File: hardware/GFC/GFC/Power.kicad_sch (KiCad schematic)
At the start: 8 parts

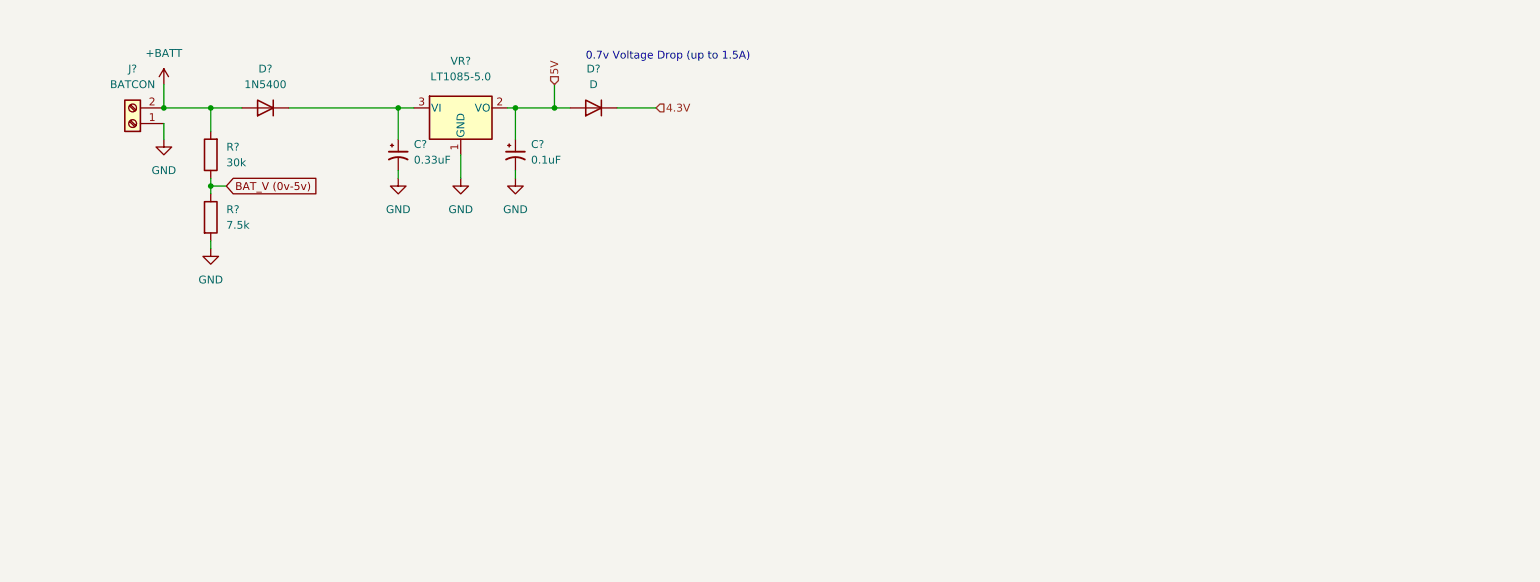
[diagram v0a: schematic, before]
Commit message: Some hardware changes, started to add footprints and part links to digikey. Switching most to SMD
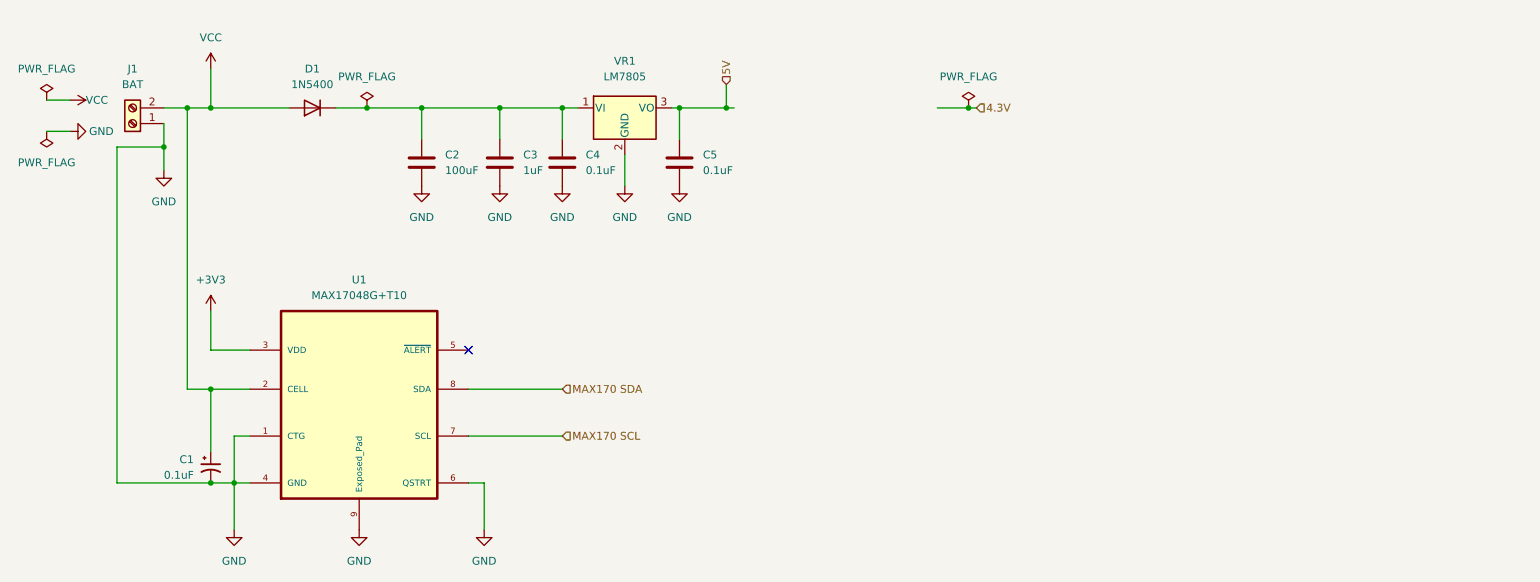
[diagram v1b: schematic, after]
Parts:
- removed C?: 0.1uF, symbol Device:C_Polarized_Small_US
- removed C?: 0.33uF, symbol Device:C_Polarized_Small_US
- removed D?: D, symbol Device:D
- removed R?: 7.5k, symbol Device:R
- removed R?: 30k, symbol Device:R
- added C1: 0.1uF, Capacitor_SMD:C_0603_1608Metric_Pad1.08x0.95mm_HandSolder, symbol Device:C_Polarized_Small_US
- added C2: 100uF, Capacitor_THT:CP_Radial_D6.3mm_P2.50mm, symbol Device:C
- added C3: 1uF, Capacitor_SMD:C_0603_1608Metric_Pad1.08x0.95mm_HandSolder, symbol Device:C
- added C4, C5: 0.1uF, Capacitor_SMD:C_0603_1608Metric_Pad1.08x0.95mm_HandSolder, symbol Device:C
- added U1: MAX17048G+T10, MAX17048G_T10:SON50P200X200X80-9N, symbol MAX17048G_T10:MAX17048G+T10
- D1: renamed from D?; footprint Diode_THT:D_DO-201AD_P15.24mm_Horizontal -> Diode_THT:D_DO-15_P12.70mm_Horizontal; Digikey (none) -> https://www.digikey.com/short/p7bpz43m; Unit Price (none) -> 0.38
- J1: renamed from J?; value BATCON -> BAT; footprint TerminalBlock_4Ucon:TerminalBlock_4Ucon_1x02_P3.50mm_Horizontal -> TerminalBlock_Phoenix:TerminalBlock_Phoenix_PT-1,5-2-5.0-H_1x02_P5.00mm_Horizontal; Digikey (none) -> https://www.digikey.com/short/tr2hdfmv; Unit Price (none) -> 0.54
- VR1: renamed from VR?; value LT1085-5.0 -> LM7805; footprint Package_TO_SOT_SMD:TO-263-2 -> Package_TO_SOT_SMD:TO-263-3_TabPin2; symbol Regulator_Linear:LT1085-5.0 -> Regulator_Linear:LM7805_TO220; Digikey (none) -> https://www.digikey.com/short/v9qc8bdj; Unit Price (none) -> 1.97
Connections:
- net 5V: now also VR1.3 (VO), C5.1; no longer VR1.2 (VO)
- net GND: now also VR1.2 (GND), C1.2, C2.2, C3.2, C4.2, C5.2, U1.1 (CTG), U1.4 (GND), U1.6 (QSTRT), U1.9 (Exposed_Pad); no longer VR1.1 (GND)
- net at D1.1 (K): now also VR1.1 (VI), C2.1, C3.1, C4.1; no longer VR1.3 (VI)
- net +BATT renamed VCC
- net VCC: now also C1.1, U1.2 (CELL)
- new net +3V3: U1.3 (VDD)
- new net MAX170 SCL: U1.7 (SCL)
- new net MAX170 SDA: U1.8 (SDA)
- no-connect marks 0 -> 1
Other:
- note removed: "0.7v Voltage Drop (up to 1.5A)"
- moved on the sheet: D1, VR1

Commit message: Updated footprints - Started work on PCB layout
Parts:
- added C18: 0.33uF, Capacitor_SMD:C_0603_1608Metric_Pad1.08x0.95mm_HandSolder, symbol Device:C
- added C19: 10uF, Capacitor_SMD:C_0805_2012Metric_Pad1.18x1.45mm_HandSolder, symbol Device:C_Polarized
- added R11: 40k, Resistor_SMD:R_1206_3216Metric_Pad1.30x1.75mm_HandSolder, symbol Device:R
- added R12: 100k, Resistor_SMD:R_0603_1608Metric_Pad0.98x0.95mm_HandSolder, symbol Device:R
- added U5: LD29150PTR, PPAK_50PTR_STM, symbol LDV VReg:LD29150PTR
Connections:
- net 4.3V: now also C19.1, R12.1, U5.4 (OUTPUT)
- net 5V: now also C18.1, U5.2 (INPUT)
- net GND: now also J1.2 (Pin_2), C18.2, C19.2, R11.2, U5.3 (GND); no longer J1.1 (Pin_1)
- net VCC: now also J1.1 (Pin_1); no longer J1.2 (Pin_2)
- new net: R11.1, R12.2, U5.5 (ADJ/N-C-*)
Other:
- moved on the sheet: J1

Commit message: Sync PCB
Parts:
- VR2: renamed from U5; footprint PPAK_50PTR_STM -> footprints:LD29150PTR
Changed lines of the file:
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@@
   (symbol (lib_id "LDV VReg:LD29150PTR") (at 189.23 49.53 0) (unit 1)
     (in_bom yes) (on_board yes) (fields_autoplaced)
-    (property "Reference" "U5" (id 0) (at 214.63 38.1 0)
+    (property "Reference" "VR2" (id 0) (at 214.63 38.1 0)
       (effects (font (size 1.524 1.524)))
     )
@@
       (effects (font (size 1.524 1.524)))
     )
-    (property "Footprint" "PPAK_50PTR_STM" (id 2) (at 214.63 43.434 0)
+    (property "Footprint" "footprints:LD29150PTR" (id 2) (at 214.63 43.434 0)
       (effects (font (size 1.524 1.524)) hide)
     )

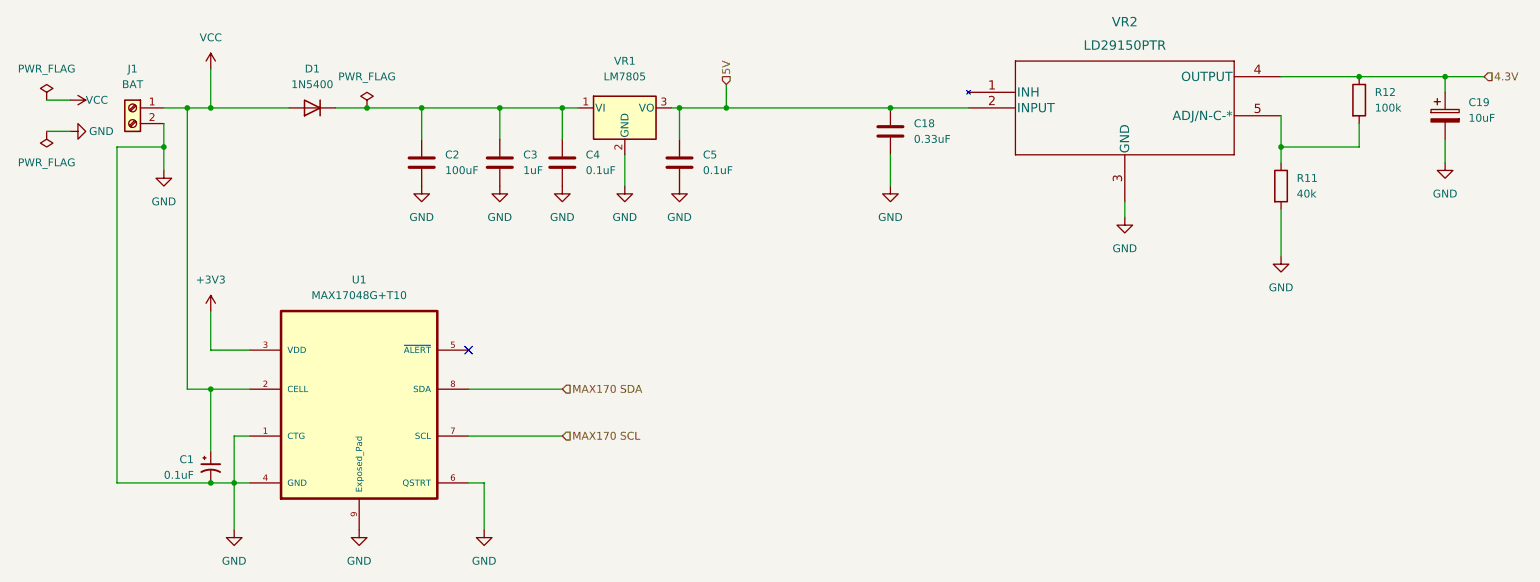
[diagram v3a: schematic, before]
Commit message: Schematic Update - ADC/DAC & GPIO Config EEPROM
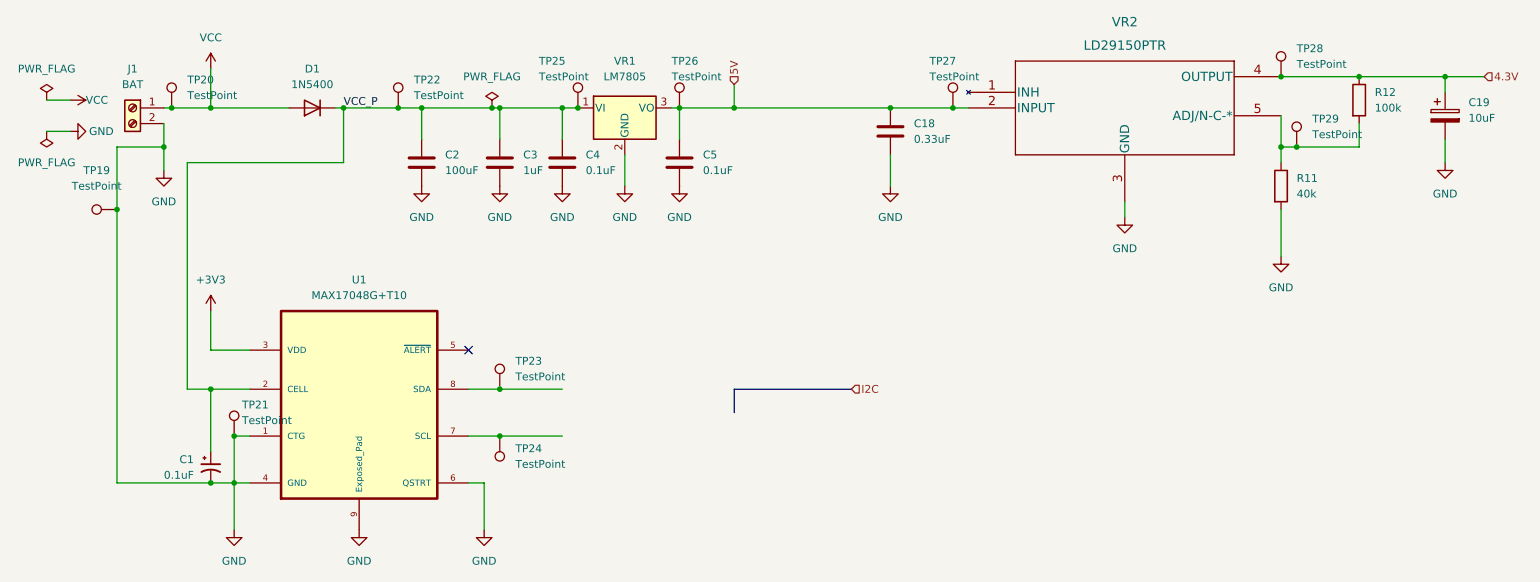
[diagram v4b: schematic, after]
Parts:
- added TP19, TP20, TP21, TP22, TP23, TP24, TP25, TP26, TP27, TP28, TP29: TestPoint, TestPoint:TestPoint_Pad_D1.0mm, symbol Connector:TestPoint
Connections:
- net 4.3V: now also TP28.1
- net 5V: now also TP26.1, TP27.1
- net GND: now also TP19.1, TP21.1
- net VCC: now also TP20.1; no longer C1.1, U1.2 (CELL)
- net VCC_P: now reaches C2.1, C3.1, C4.1, D1.1 (K), VR1.1 (VI)
- net VCC_P: now also C1.1, U1.2 (CELL), TP22.1, TP25.1
- net at R11.1, R12.2, VR2.5 (ADJ/N-C-*): now also TP29.1
- net MAX170 SCL: no longer names the net of U1.7 (SCL)
- net MAX170 SCL: now also TP24.1
- net MAX170 SDA: no longer names the net of U1.8 (SDA)
- net MAX170 SDA: now also TP23.1

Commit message: sync
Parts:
- removed TP19, TP20, TP21, TP22, TP23, TP24, TP25, TP26, TP27, TP28, TP29: TestPoint, TestPoint:TestPoint_Pad_D1.0mm, symbol Connector:TestPoint
- added TP29, TP30, TP31, TP32, TP33, TP34, TP35, TP36: Test Point, TestPoint:TestPoint_Pad_D1.0mm, symbol Connector:TestPoint_Small
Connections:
- net +3V3: now also TP30.1
- net 4.3V: now also TP36.1
- net 5V: now also TP34.1
- net VCC: now also C1.1, U1.2 (CELL), TP29.1
- net VCC_P: now also TP31.1; no longer C1.1, U1.2 (CELL)
- net I2C0.SDA: now reaches U1.8 (SDA)
- net I2C0.SDA: now also TP32.1
- net I2C0.SCL: now reaches U1.7 (SCL)
- net I2C0.SCL: now also TP33.1
- net at R11.1, R12.2, VR2.5 (ADJ/N-C-*): now also TP35.1
